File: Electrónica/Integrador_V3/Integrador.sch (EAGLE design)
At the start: 12 parts, among them J1 22-27-2031-03, U1 OPA4228PA, X3 SMA-142-0711-821/826, X4 SMA-142-0711-821/826

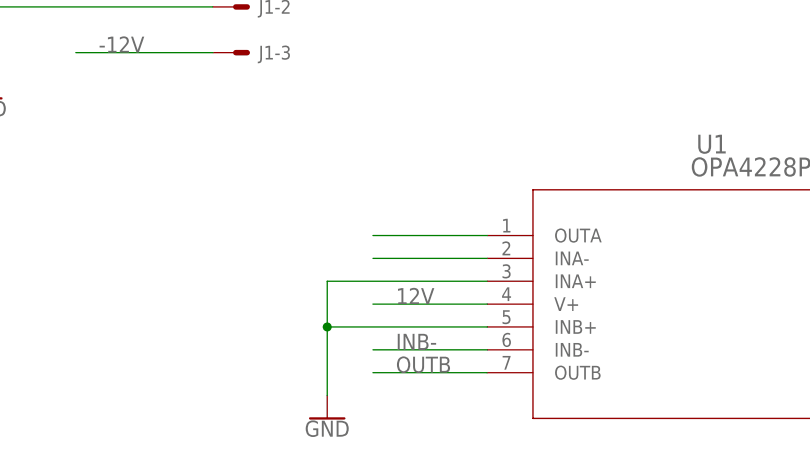
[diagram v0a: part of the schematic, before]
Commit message: Integrador con 5.2 cm de largo y usando el opa4228
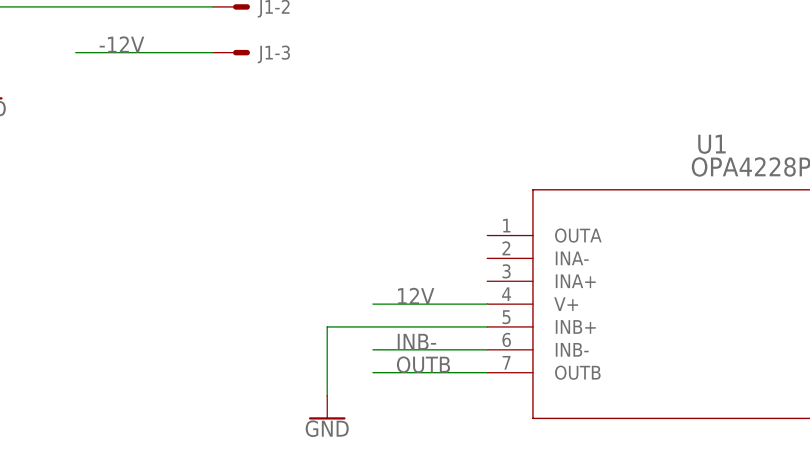
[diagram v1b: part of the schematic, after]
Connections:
- removed net N$10: U1.OUTA
- removed net N$11: U1.INA-
- net GND: no longer U1.INA+
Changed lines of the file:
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@@
 </segment>
 <segment>
-<pinref part="U1" gate="A" pin="INA+"/>
-<wire x1="30.48" y1="-7.62" x2="12.7" y2="-7.62" width="0.1524" layer="91"/>
 <pinref part="GND3" gate="1" pin="GND"/>
-<wire x1="12.7" y1="-7.62" x2="12.7" y2="-12.7" width="0.1524" layer="91"/>
 <pinref part="U1" gate="A" pin="INB+"/>
 <wire x1="12.7" y1="-12.7" x2="12.7" y2="-20.32" width="0.1524" layer="91"/>
 <wire x1="30.48" y1="-12.7" x2="12.7" y2="-12.7" width="0.1524" layer="91"/>
-<junction x="12.7" y="-12.7"/>
 </segment>
 <segment>
@@
 </segment>
 </net>
-<net name="N$10" class="0">
-<segment>
-<pinref part="U1" gate="A" pin="OUTA"/>
-<wire x1="30.48" y1="-2.54" x2="17.78" y2="-2.54" width="0.1524" layer="91"/>
-</segment>
-</net>
-<net name="N$11" class="0">
-<segment>
-<pinref part="U1" gate="A" pin="INA-"/>
-<wire x1="30.48" y1="-5.08" x2="17.78" y2="-5.08" width="0.1524" layer="91"/>
-</segment>
-</net>
